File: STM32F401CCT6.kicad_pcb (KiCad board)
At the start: 2 copper layers, 52 x 22.9 mm, 37 parts, among them J1 USB_OTG, J2 Conn_02x03_Odd_Even, J3 Conn_01x20_des, J4 Conn_01x05_desc, J5 Conn_01x20, SW1 SW_Push, U1 MIC5219-3.3, U2 STM32F401CCT6, U3 USBLC6-2SC6, Y1 32.786K, Y2 8MHz

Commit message: Added extra capacitor between VDD and GND (VFFA-VSSA)
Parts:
- added C15: 4.7u,0603, Capacitors_SMD:C_0603, B.Cu at (90.4, 106.5)
- added C16: 0.1uF,0603, Capacitors_SMD:C_0603, B.Cu at (79.5, 106.5)
- added C17: 104,0603, Capacitors_SMD:C_0603, B.Cu at (119.4, 114.5)
- added C18: 104,0603, Capacitors_SMD:C_0603, B.Cu at (108.3, 114.5)
- added C19: 0.1uF,0603, Capacitors_SMD:C_0603, B.Cu at (105.9, 112.2)
- C10, C11: value 104,0603 -> 4.7uF,0603
- U2: value STM32F401CCT6 -> STM32FxxxCx
- moved C11 5.29 mm to (94.3, 109.3)
- moved C12 3.60 mm to (97.9, 109.3)
- moved C10 1.77 mm to (99.6, 109.3)
- moved R9 1.37 mm to (76.1, 106.4)
- moved R4 0.24 mm to (82.6, 109.1)
- moved R3 0.14 mm to (80.8, 109.1)
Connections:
- net /PB11 renamed /PB11/VCAP1
- J1 pad 6: (no net) -> GND
- U2 pad 0: (no net) -> GND
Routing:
- net VCC: track 189.2 -> 305.3 mm
- net GND: track 186.7 -> 287.3 mm, vias 11 -> 16
- net +5V: track 61.2 -> 99.9 mm, vias 2 -> 3
- net /RESET: track 91.8 -> 84.5 mm, vias 3 -> 4
- net /PB11/VCAP1: track 10.6 -> 16.0 mm, vias 0 -> 1
- net /BOOT1: track 12.5 -> 11.0 mm
- net /SWDIO: track 32.8 -> 34.1 mm
- net Net-(C2-Pad1): track 7.41 -> 6.65 mm
- net /PA9: track 9.05 -> 8.54 mm

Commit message: Fixed the pad near tracks error (reallocated the QFN)
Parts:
- C10, C11: value 4.7uF,0603 -> 104,0603
- U2: value STM32FxxxCx -> STM32F401CCT6
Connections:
- net /PB11/VCAP1 renamed /PB11
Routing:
- net VCC: track 305.3 -> 295.5 mm
- net /RESET: track 84.5 -> 92.3 mm
- net +5V: track 99.9 -> 95.2 mm
- net GND: track 287.3 -> 283.3 mm
- net /PB11: track 16.0 -> 12.1 mm
- net /SWDIO: track 34.1 -> 33.4 mm
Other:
- net class new: via_dia 0.45 -> 0.453

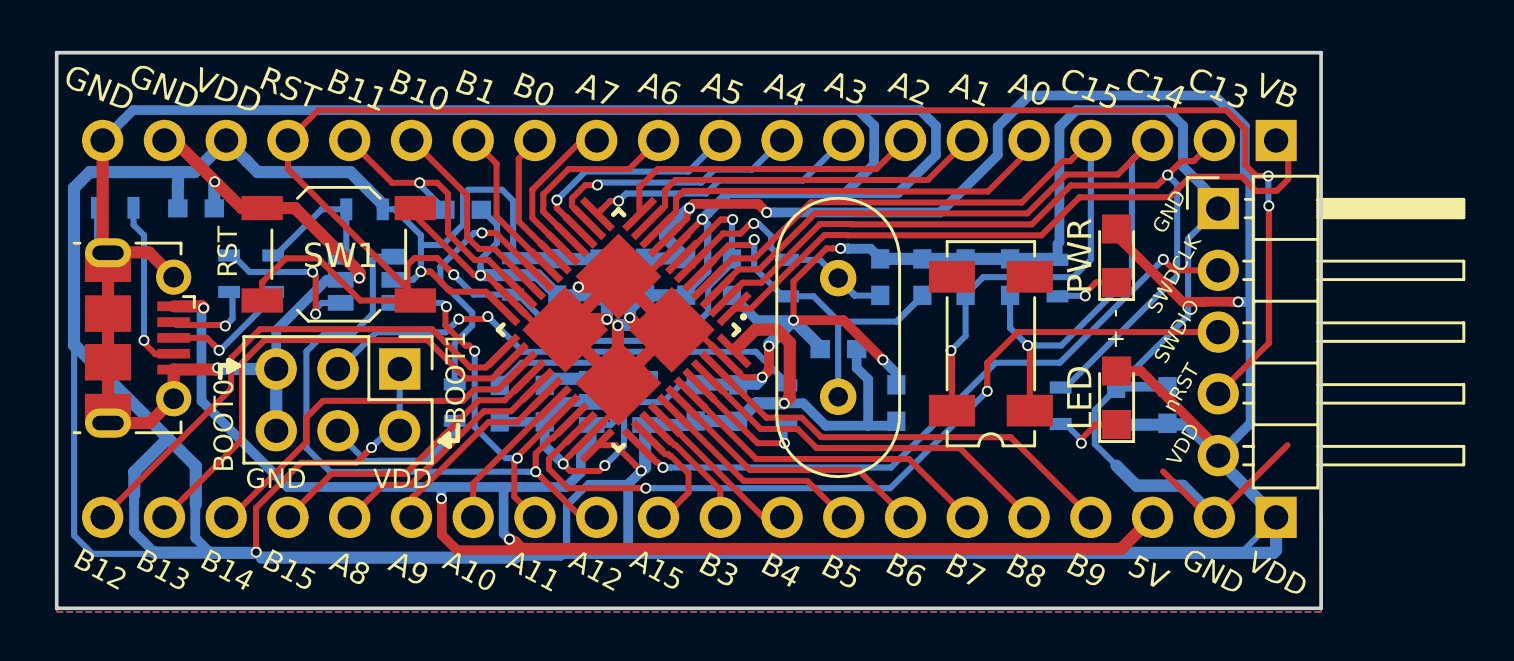
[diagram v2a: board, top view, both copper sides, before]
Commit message: Change pin20 to Pwr Enable and added a resistor on it
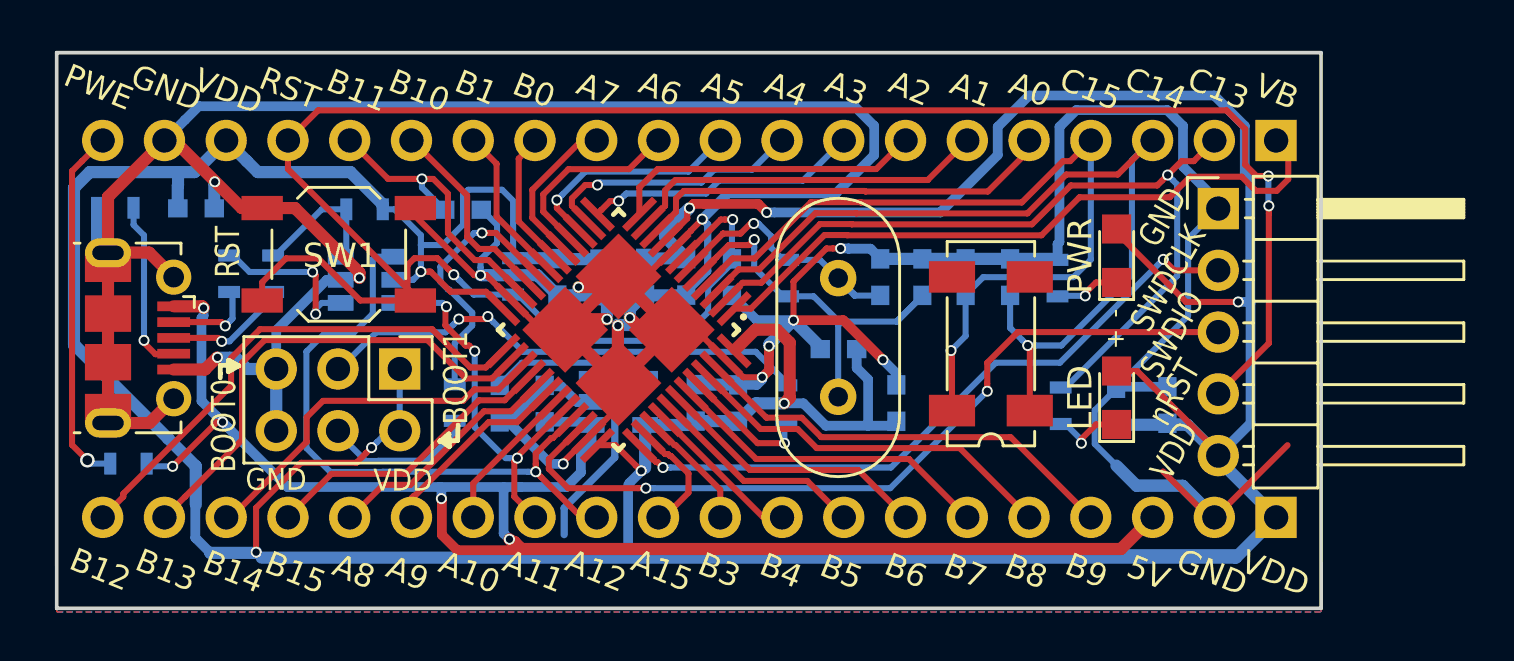
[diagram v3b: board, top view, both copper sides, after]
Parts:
- added R11: 10K, Resistors_SMD:R_0603, B.Cu at (76.7, 117.0)
- C10, C11: value 104,0603 -> 4.7uF,0603
- turned C1 to 90 degrees
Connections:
- net /PB11 renamed /PB11/VCAP1
- J3 pad 20: GND -> /PWR_EN
- U1 pad 3: +5V -> /PWR_EN
- Y1 pad 2: (no net) -> /PC15
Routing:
- net VCC: track 295.5 -> 249.0 mm
- net GND: track 283.3 -> 257.3 mm, vias 16 -> 15
- net /PWR_EN: track 0.00 -> 23.1 mm, vias 0 -> 1
- net +5V: track 95.2 -> 95.5 mm, vias 3 -> 5
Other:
- board text added: "PWE"

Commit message: Re-routed (prioritised D+ D- SWDIO SWCLK) by reducing the track length and via along the tracks.
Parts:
- moved R9 5.15 mm to (75.9, 111.6), turned to 270 degrees
- moved R3 1.85 mm to (82.4, 108.2), turned to 180 degrees
- moved R6 1.10 mm to (113.9, 114.5)
- moved R4 1.01 mm to (82.4, 110.1), turned to 180 degrees
- moved R8 0.54 mm to (90.6, 114.5)
- moved C2 0.37 mm to (92.3, 114.5)
- moved C1 0.16 mm to (94.0, 114.5)
- moved C6 0.15 mm to (113.1, 109.3), turned to 270 degrees
- moved J1 0.15 mm to (76.2, 111.6)
- moved SW1 0.13 mm to (85.3, 108.2)
- moved C7 0.12 mm to (111.2, 109.3), turned to 270 degrees
- moved R5 0.08 mm to (115.0, 109.3)
- moved C18 0.06 mm to (108.3, 114.5)
- moved C17 0.05 mm to (119.4, 114.6), turned to 270 degrees
- turned C14 to 270 degrees
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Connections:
- U3 pad 1: Net-(R3-Pad1) -> /PA11
- U3 pad 3: Net-(R10-Pad1) -> /PA12
- U3 pad 4: /PA12 -> Net-(R10-Pad1)
- U3 pad 6: /PA11 -> Net-(R3-Pad1)
- Y1 pad 2: /PC15 -> (no net)
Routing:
- net VCC: track 249.0 -> 199.4 mm, vias 8 -> 10
- net +5V: track 95.5 -> 66.8 mm, vias 5 -> 4
- net GND: track 257.3 -> 229.0 mm, vias 15 -> 17
- net /PWR_EN: track 23.1 -> 48.0 mm, vias 1 -> 2
- net /PC14: track 37.3 -> 26.6 mm, vias 1 -> 2
- net /PA12: track 26.7 -> 17.5 mm
- net /PC15: track 33.9 -> 24.7 mm, vias 1 -> 2
- net /ID: track 7.59 -> 2.69 mm
- net Net-(R3-Pad1): track 6.71 -> 2.32 mm, vias 2 -> 0
- net Net-(J2-Pad3): track 20.6 -> 24.0 mm
- net Net-(J2-Pad4): track 6.28 -> 8.85 mm, vias 0 -> 2
- net /PA11: track 15.6 -> 17.8 mm, vias 3 -> 1
- net /SWDCLK: track 27.9 -> 30.0 mm, vias 2 -> 1
- net /PC13: track 33.8 -> 31.9 mm
- net /RESET: track 92.3 -> 90.5 mm
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
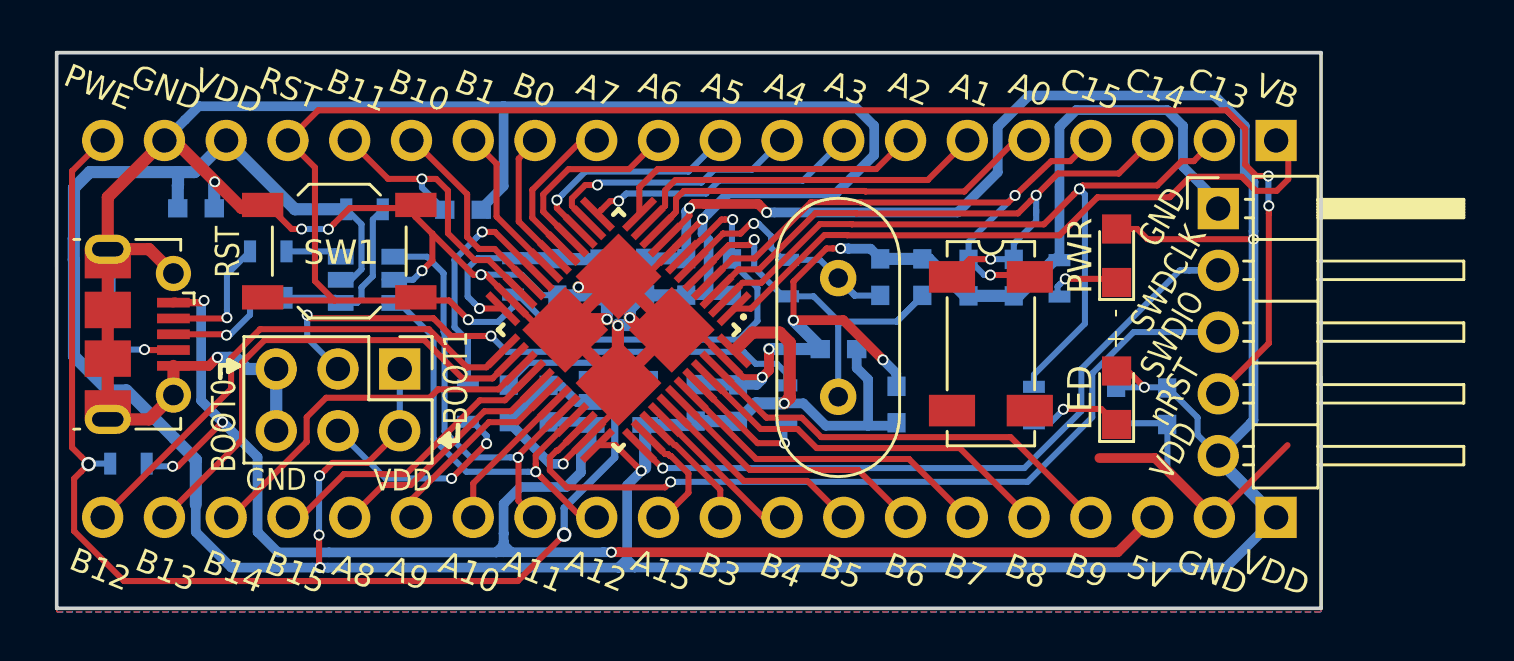
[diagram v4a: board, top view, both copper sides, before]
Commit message: Changed the via size to 0.453/0.3 mm
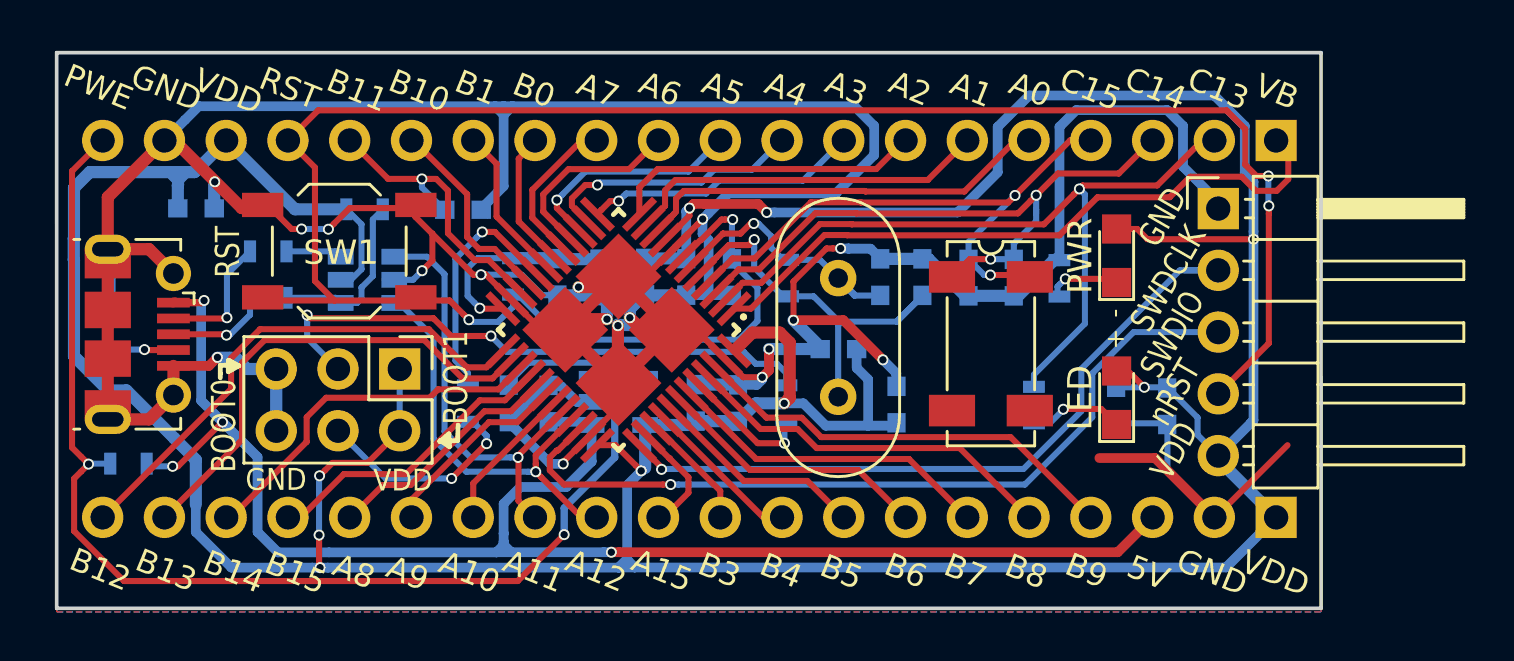
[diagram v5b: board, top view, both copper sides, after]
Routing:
- net VCC: track 199.4 -> 200.8 mm
- net GND: track 229.0 -> 230.0 mm

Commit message: Renamed VCC to VDD
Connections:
- net VCC renamed /VDD
